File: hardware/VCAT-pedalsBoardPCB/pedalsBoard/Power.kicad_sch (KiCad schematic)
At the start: 2 parts, among them J5 Conn_01x02

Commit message: meow
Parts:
- removed J5: Conn_01x02, Package_DFN_QFN:QFN-20-1EP_5x5mm_P0.65mm_EP3.35x3.35mm, symbol Connector_Generic:Conn_01x02
- added R2: 16k, symbol Device:R
- added R3: 4.7K, symbol Device:R
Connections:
- net P_IN: now reaches F4.2
- new net 12VBuck/V_out_5V: R2.1
- new net Power_Mux/MX_GND: R3.2
- new net Power_Mux/PR1: R2.2, R3.1
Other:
- sheet PowerProtection renamed PP
- added sheet Power_Mux (Power_Mux.kicad_sch)
- note added: "POWER"
- moved on the sheet: F4

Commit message: test
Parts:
- added JP2: SolderJumper_2_Open, symbol Jumper:SolderJumper_2_Open
- added TP1: TP_12V, symbol Connector:TestPoint
- added TP2: TP_5V_VIN1, symbol Connector:TestPoint
- added TP3: TP_5V_MUX, symbol Connector:TestPoint
- added TP4: TP_3.3V, symbol Connector:TestPoint
- F4: footprint 3557-2 -> MyParts:3557-2
- R2, R3: footprint (none) -> Resistor_SMD:R_0603_1608Metric
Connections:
- net Power_Mux/MX_GND is gone; now on net GND: R3.2
- net 12V: now also JP2.2 (B), TP1.1
- net 3.3V: now also TP4.1
- net 5V: now also TP3.1
- net PP/Vin: now also JP2.1 (A)
- net 12VBuck/V_out_5V renamed 5V_Buck
- net 5V_Buck: now also TP2.1
- net P_IN renamed V_IN
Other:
- note added: "Both Resistors are using the Resistor_0603_1608 Same size fp right?"
- moved on the sheet: F4, R2, R3

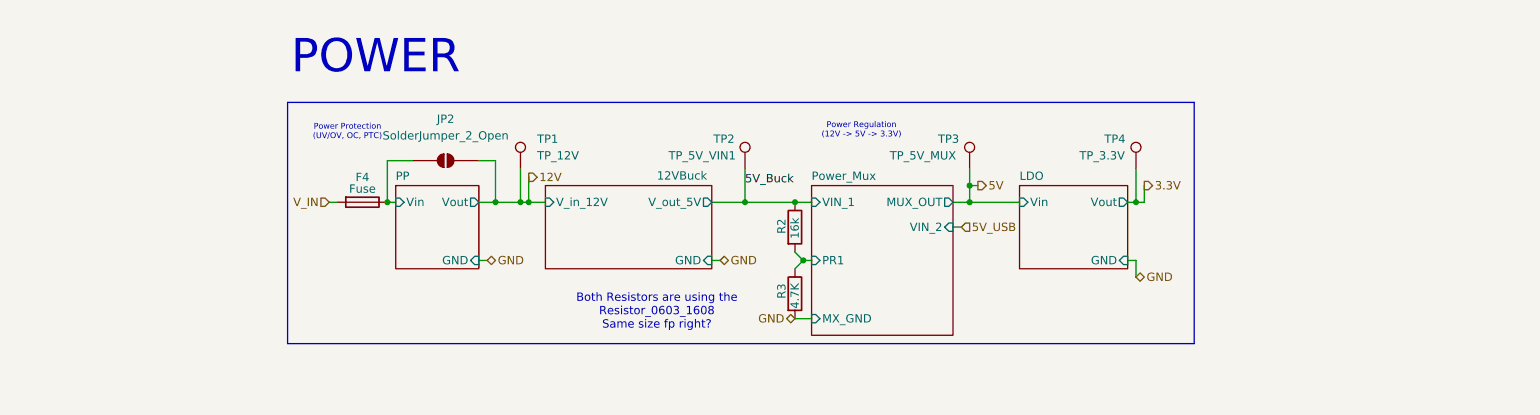
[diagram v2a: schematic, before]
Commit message: addressed review, brake switch on slack
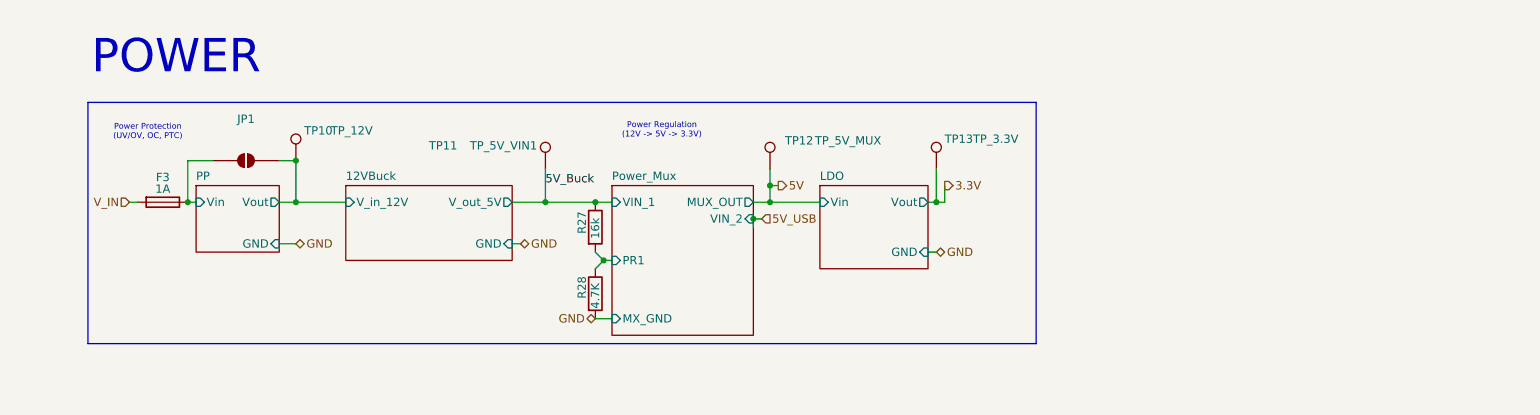
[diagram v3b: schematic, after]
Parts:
- removed TP1: TP_12V, symbol Connector:TestPoint
- removed TP2: TP_5V_VIN1, symbol Connector:TestPoint
- removed TP3: TP_5V_MUX, symbol Connector:TestPoint
- removed TP4: TP_3.3V, symbol Connector:TestPoint
- added TP10: TP_12V, TestPoint:TestPoint_Loop_D1.80mm_Drill1.0mm_Beaded, symbol lhrs_misc:Multimeter_TP
- added TP11: TP_5V_VIN1, TestPoint:TestPoint_Loop_D1.80mm_Drill1.0mm_Beaded, symbol lhrs_misc:Multimeter_TP
- added TP12: TP_5V_MUX, TestPoint:TestPoint_Loop_D1.80mm_Drill1.0mm_Beaded, symbol lhrs_misc:Multimeter_TP
- added TP13: TP_3.3V, TestPoint:TestPoint_Loop_D1.80mm_Drill1.0mm_Beaded, symbol lhrs_misc:Multimeter_TP
- F3: renamed from F4; value Fuse -> 1A
- renumbered JP2 to JP1, R2 to R27, R3 to R28
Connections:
- net 3.3V: now also TP13.1
- net 5V: now also TP12.1
- net 5V_Buck: now also TP11.1
- net 12V renamed 12VBuck/V_in_12V
- net 12VBuck/V_in_12V: now also TP10.1
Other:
- sheet PP: file PowerProtection.kicad_sch -> PP.kicad_sch
- note removed: "Both Resistors are using the Resistor_0603_1608 Same size fp right?"
- moved on the sheet: F3, JP1, R27, R28

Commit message: hopefully final before layout
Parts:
- JP1: footprint (none) -> Connector_PinHeader_2.54mm:PinHeader_1x02_P2.54mm_Vertical
- R27, R28: footprint Resistor_SMD:R_0603_1608Metric -> Resistor_SMD:R_0603_1608Metric_Pad0.98x0.95mm_HandSolder
- TP10, TP11, TP12, TP13: footprint TestPoint:TestPoint_Loop_D1.80mm_Drill1.0mm_Beaded -> LHRS_Special:TestPoint_HEX_3mmID
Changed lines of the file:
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@@
 	(rectangle
 		(start 36.83 53.34)
-		(end 181.61 90.17)
+		(end 181.61 99.06)
 		(stroke
 			(width 0)
@@
 	)
 	(junction
-		(at 138.43 71.12)
-		(diameter 0)
-		(color 0 0 0 0)
-	)
-	(junction
 		(at 68.58 62.23)
 		(diameter 0)
@@
 	(wire
 		(pts
-			(xy 167.64 66.04) (xy 167.64 68.58)
-		)
-		(stroke
-			(width 0)
-			(type default)
-		)
-	)
-	(wire
-		(pts
 			(xy 68.58 62.23) (xy 68.58 68.58)
 		)
@@
 	(wire
 		(pts
-			(xy 166.37 68.58) (xy 167.64 68.58)
+			(xy 166.37 68.58) (xy 168.91 68.58)
 		)
 		(stroke
@@
 		(pts
 			(xy 166.37 63.5) (xy 166.37 68.58)
-		)
-		(stroke
-			(width 0)
-			(type default)
-		)
-	)
-	(wire
-		(pts
-			(xy 138.43 71.12) (xy 138.43 72.39)
 		)
 		(stroke
@@
 	(hierarchical_label "3.3V"
 		(shape output)
-		(at 167.64 66.04 0)
+		(at 168.91 68.58 0)
 		(effects
 			(font
@@
 		)
 		(property "Value" "TP_12V"
-			(at 73.914 57.658 0)
-			(show_name no)
-			(do_not_autoplace no)
-			(effects
-				(font
-					(size 1.27 1.27)
-				)
-				(justify left)
-			)
-		)
-		(property "Footprint" "TestPoint:TestPoint_Loop_D1.80mm_Drill1.0mm_Beaded"
+			(at 74.93 57.658 0)
+			(show_name no)
+			(do_not_autoplace no)
+			(effects
+				(font
+					(size 1.27 1.27)
+				)
+				(justify left)
+			)
+		)
+		(property "Footprint" "LHRS_Special:TestPoint_HEX_3mmID"
 			(at 68.58 57.15 0)
 			(hide yes)
@@
 			)
 		)
-		(property "Footprint" "TestPoint:TestPoint_Loop_D1.80mm_Drill1.0mm_Beaded"
+		(property "Footprint" "LHRS_Special:TestPoint_HEX_3mmID"
 			(at 106.68 58.42 0)
 			(hide yes)
@@
 			)
 		)
-		(property "Footprint" ""
+		(property "Footprint" "Connector_PinHeader_2.54mm:PinHeader_1x02_P2.54mm_Vertical"
 			(at 60.96 62.23 0)
 			(hide yes)
@@
 			)
 		)
-		(property "Footprint" "TestPoint:TestPoint_Loop_D1.80mm_Drill1.0mm_Beaded"
+		(property "Footprint" "LHRS_Special:TestPoint_HEX_3mmID"
 			(at 166.37 58.42 0)
 			(hide yes)
@@
 			)
 		)
-		(property "Footprint" "Resistor_SMD:R_0603_1608Metric"
+		(property "Footprint" "Resistor_SMD:R_0603_1608Metric_Pad0.98x0.95mm_HandSolder"
 			(at 112.522 82.55 90)
 			(hide yes)
@@
 			)
 		)
-		(property "Footprint" "TestPoint:TestPoint_Loop_D1.80mm_Drill1.0mm_Beaded"
+		(property "Footprint" "LHRS_Special:TestPoint_HEX_3mmID"
 			(at 140.97 58.42 0)
 			(hide yes)
@@
 			)
 		)
-		(property "Footprint" "Resistor_SMD:R_0603_1608Metric"
+		(property "Footprint" "Resistor_SMD:R_0603_1608Metric_Pad0.98x0.95mm_HandSolder"
 			(at 112.522 72.39 90)
 			(hide yes)
@@
 	(sheet
 		(at 116.84 66.04)
-		(size 21.59 22.86)
+		(size 21.59 30.48)
 		(exclude_from_sim no)
 		(in_bom yes)
@@
 		)
 		(property "Sheetfile" "Power_Mux.kicad_sch"
-			(at 116.84 89.4846 0)
+			(at 116.84 97.1046 0)
 			(hide yes)
 			(show_name no)
@@
 	)
 	(sheet
-		(at 76.2 66.04)
-		(size 25.4 11.43)
+		(at 148.59 66.04)
+		(size 16.51 12.7)
 		(exclude_from_sim no)
 		(in_bom yes)
@@
 			(color 0 0 0 0)
 		)
-		(property "Sheetname" "12VBuck"
-			(at 76.2 65.3284 0)
+		(property "Sheetname" "LDO"
+			(at 148.59 65.3284 0)
 			(show_name no)
 			(do_not_autoplace no)
@@
 			)
 		)
-		(property "Sheetfile" "12VBuck.kicad_sch"
-			(at 76.2 78.0546 0)
+		(property "Sheetfile" "LDO.kicad_sch"
+			(at 148.59 79.3246 0)
 			(hide yes)
 			(show_name no)
@@
 		)
 		(pin "GND" input
-			(at 101.6 74.93 0)
+			(at 165.1 76.2 0)
 			(effects
 				(font
@@
 			)
 		)
-		(pin "V_in_12V" input
-			(at 76.2 68.58 180)
-			(effects
-				(font
-					(size 1.27 1.27)
-				)
-				(justify left)
-			)
-		)
-		(pin "V_out_5V" output
-			(at 101.6 68.58 0)
+		(pin "Vin" input
+			(at 148.59 68.58 180)
+			(effects
+				(font
+					(size 1.27 1.27)
+				)
+				(justify left)
+			)
+		)
+		(pin "Vout" output
+			(at 165.1 68.58 0)
 			(effects
 				(font
@@
 			(project "pedalsBoard"
 				(path "/423853f6-a5c6-4d97-9a9a-db6f143664c7/26d9f075-73a6-4044-b4f9-8fe225c47fcc"
-					(page "11")
+					(page "2")
 				)
 			)
@@
 	)
 	(sheet
-		(at 148.59 66.04)
-		(size 16.51 12.7)
+		(at 76.2 62.23)
+		(size 25.4 15.24)
 		(exclude_from_sim no)
 		(in_bom yes)
@@
 			(color 0 0 0 0)
 		)
-		(property "Sheetname" "LDO"
-			(at 148.59 65.3284 0)
+		(property "Sheetname" "12VBuck"
+			(at 76.2 61.5184 0)
 			(show_name no)
 			(do_not_autoplace no)
@@
 			)
 		)
-		(property "Sheetfile" "LDO.kicad_sch"
-			(at 148.59 79.3246 0)
-			(hide yes)
+		(property "Sheetfile" "12VBuck.kicad_sch"
+			(at 76.2 78.0546 0)
 			(show_name no)
 			(do_not_autoplace no)
@@
 		)
 		(pin "GND" input
-			(at 165.1 76.2 0)
+			(at 101.6 74.93 0)
 			(effects
 				(font
@@
 			)
 		)
-		(pin "Vin" input
-			(at 148.59 68.58 180)
-			(effects
-				(font
-					(size 1.27 1.27)
-				)
-				(justify left)
-			)
-		)
-		(pin "Vout" output
-			(at 165.1 68.58 0)
+		(pin "V_in_12V" input
+			(at 76.2 68.58 180)
+			(effects
+				(font
+					(size 1.27 1.27)
+				)
+				(justify left)
+			)
+		)
+		(pin "V_out_5V" output
+			(at 101.6 68.58 0)
 			(effects
 				(font
@@
 			(project "pedalsBoard"
 				(path "/423853f6-a5c6-4d97-9a9a-db6f143664c7/26d9f075-73a6-4044-b4f9-8fe225c47fcc"
-					(page "2")
-				)
-			)
+					(page "7")
+				)
+			)

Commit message: tweaked some power labels
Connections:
- net 12VBuck/V_in_12V renamed +12V_PP
- net 5V_Buck renamed 12VBuck/V_out_5V
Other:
- note removed: "Power Protection (UV/OV, OC, PTC)"
- note removed: "Power Regulation (12V -> 5V -> 3.3V)"
- moved on the sheet: F3, JP1, TP10, TP11, TP12, TP13
